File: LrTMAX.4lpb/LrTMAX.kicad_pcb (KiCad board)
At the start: 4 copper layers, 100 x 100 mm, 124 parts, among them J1 USB_B_Micro, J2 SM06B-SRSS-TB, Q1 2N7002, SW1 Tact_SW_8mm, SW10 EC11_SMD, SW11 EC11_SMD, SW12 EC11_SMD, SW13 EC11_SMD, SW14 EC11_SMD, SW15 EC11_SMD, SW16 EC11_SMD, SW17 EC11_SMD, SW2 Tact_SW_8mm, SW3 Tact_SW_8mm, SW4 Tact_SW_8mm, SW5 Tact_SW_8mm, SW6 Tact_SW_8mm, SW7 Tact_SW_8mm, SW8 Tact_SW_8mm, U1 STM32F072C8Tx, U3 SSD1306_OLED_0.91, U4 SPX3819M5-L3-3TR

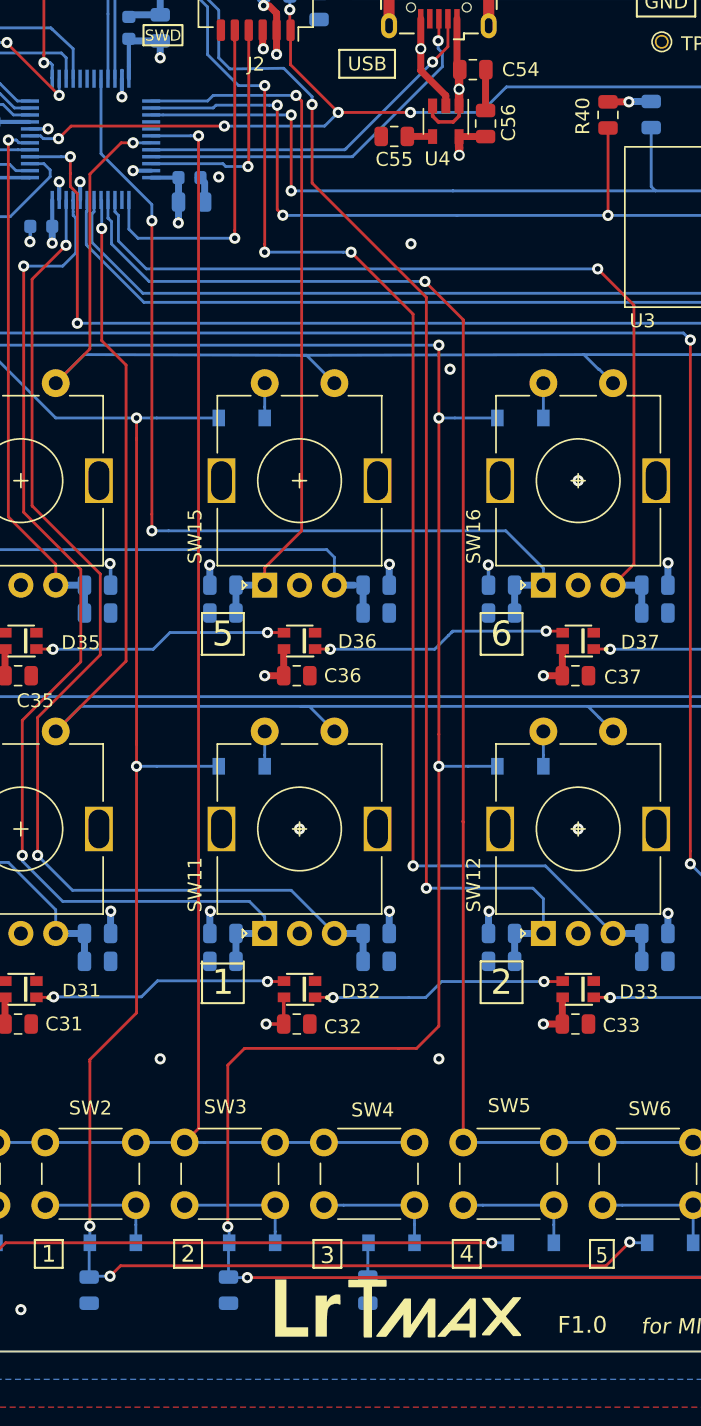
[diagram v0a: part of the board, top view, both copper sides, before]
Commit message: 0.46-4
Fix EXTI routine for ENC3.
(and first modify for F1.2 board)
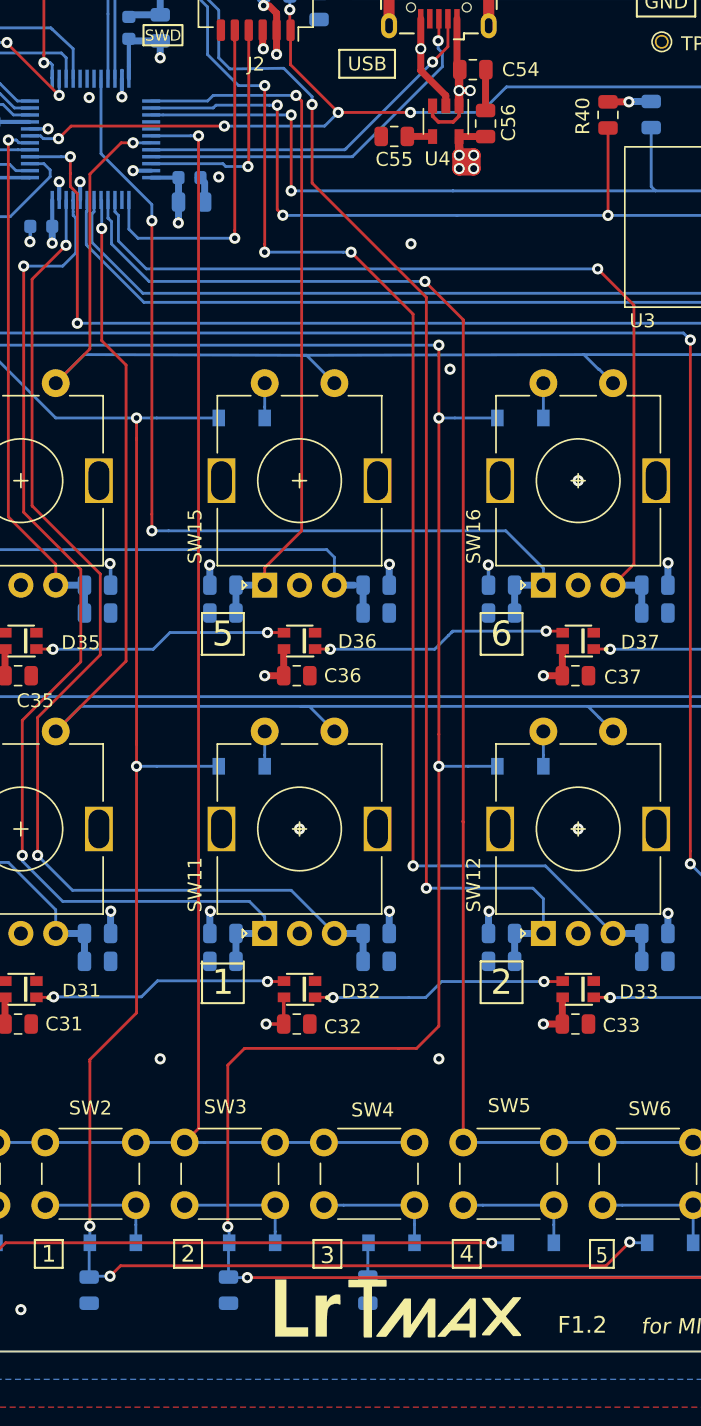
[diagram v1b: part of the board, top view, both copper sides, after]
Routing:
- net +3V3: track 70.1 -> 74.1 mm, vias 27 -> 30
- net /VBUS: track 41.4 -> 42.2 mm, vias 10 -> 11
- net GND: vias 45 -> 46
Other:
- board text added: "F1.2"
- board text removed: "F1.0"
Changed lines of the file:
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@@
     (thickness 1.6)
     (drawings 120)
-    (tracks 992)
+    (tracks 1002)
     (zones 0)
     (modules 124)
@@
     )
   )
-  (gr_text F1.0 (at 160.3 198.1) (layer F.SilkS)
+  (gr_text F1.2 (at 160.3 198.1) (layer F.SilkS)
     (effects (font (size 1.2 1.2) (thickness 0.22)))
   )
@@
   (via (at 134.2 115.7) (size 0.8) (drill 0.4) (layers F.Cu B.Cu) (net 3))
   (via (at 150.8 129.5) (size 0.8) (drill 0.4) (layers F.Cu B.Cu) (net 3))
+  (via (at 124.9 110) (size 0.8) (drill 0.4) (layers F.Cu B.Cu) (net 3))
   (segment (start 178.25 190.914213) (end 178.25 192.2) (width 0.2032) (layer B.Cu) (net 4))
   (segment (start 178.25 189.5) (end 178.25 190.914213) (width 0.2032) (layer B.Cu) (net 4))
@@
   (segment (start 137.5 132.1968) (end 137.5 130.5) (width 0.2032) (layer B.Cu) (net 8))
   (segment (start 137.5 133) (end 137.5 132.1968) (width 0.2032) (layer B.Cu) (net 8))
+  (via (at 152.5 114.141) (size 0.8) (drill 0.5) (layers F.Cu B.Cu) (net 9))
+  (via (at 151.459 115.1) (size 0.8) (drill 0.5) (layers F.Cu B.Cu) (net 9))
+  (via (at 152.5 115.1) (size 0.8) (drill 0.5) (layers F.Cu B.Cu) (net 9))
   (via (at 118.1 113) (size 0.8) (drill 0.4) (layers F.Cu B.Cu) (net 9))
   (via (at 122.25 120.45) (size 0.8) (drill 0.4) (layers F.Cu B.Cu) (net 9))
@@
   (segment (start 173.5625 145) (end 173.5625 143.5625) (width 0.5) (layer B.Cu) (net 9))
   (segment (start 173.5625 143.5625) (end 173.55 143.55) (width 0.254) (layer B.Cu) (net 9))
+  (segment (start 151.459 114.141) (end 151.459 115.1) (width 1) (layer F.Cu) (net 9))
+  (segment (start 151.459 114.141) (end 152.5 114.141) (width 1) (layer F.Cu) (net 9))
+  (segment (start 152.5 114.141) (end 152.5 115.1) (width 1) (layer F.Cu) (net 9))
+  (segment (start 152.5 115.1) (end 151.459 115.1) (width 1) (layer F.Cu) (net 9))
   (segment (start 134.9 192.25) (end 134.95 192.2) (width 0.2032) (layer B.Cu) (net 10))
   (segment (start 134.9 194.6625) (end 134.9 192.25) (width 0.2032) (layer B.Cu) (net 10))
@@
   (segment (start 151.3 104.35) (end 151.3 107.7995) (width 0.5) (layer F.Cu) (net 17) (status 30))
   (segment (start 151.3 107.7995) (end 151.5 108) (width 0.2032) (layer F.Cu) (net 17) (status 30))
-  (via (at 151.45 109.4) (size 0.8) (drill 0.5) (layers F.Cu B.Cu) (net 17))
+  (via (at 151.45 109.5) (size 0.8) (drill 0.5) (layers F.Cu B.Cu) (net 17))
   (segment (start 151.45 110.6) (end 151.45 109.4) (width 0.6) (layer F.Cu) (net 17) (status 10))
   (segment (start 151.45 108.0505) (end 151.5005 108) (width 0.2032) (layer F.Cu) (net 17) (status 30))
@@
   (via (at 117.6 176.5) (size 0.8) (drill 0.4) (layers F.Cu B.Cu) (net 17))
   (segment (start 118.8625 176.5) (end 117.6 176.5) (width 0.5) (layer F.Cu) (net 17))
+  (via (at 152.25 109.5) (size 0.8) (drill 0.5) (layers F.Cu B.Cu) (net 17))
+  (segment (start 151.45 109.5) (end 152.25 109.5) (width 0.5) (layer F.Cu) (net 17))
   (segment (start 149.55 107.45) (end 150.65 106.35) (width 0.2032) (layer F.Cu) (net 18))
   (segment (start 150.65 106.35) (end 150.65 104.35) (width 0.2032) (layer F.Cu) (net 18) (status 20))
@@
   )
   (zone (net 0) (net_name "") (layer F.Cu) (hatch edge 0.508)
-    (connect_pads (clearance 0.3))
-    (min_thickness 0.254)
-    (keepout (tracks allowed) (vias allowed) (copperpour not_allowed))
-    (fill (arc_segments 32) (thermal_gap 0.508) (thermal_bridge_width 0.508))
-    (polygon
-      (pts
-        (xy 150.7 108.2) (xy 150.4 108.2125) (xy 150.1 108.225) (xy 149.5 108.25) (xy 149.5 105.55)
-        (xy 150.7 105.55)
-      )
-    )
-  )
-  (zone (net 0) (net_name "") (layer F.Cu) (hatch edge 0.508)
     (connect_pads (clearance 0.254))
     (min_thickness 0.254)
@@
       )
     )
+  )
+  (zone (net 0) (net_name "") (layer F.Cu) (hatch edge 0.508)
+    (connect_pads (clearance 0.3))
+    (min_thickness 0.254)
+    (keepout (tracks allowed) (vias allowed) (copperpour not_allowed))
+    (fill (arc_segments 32) (thermal_gap 0.508) (thermal_bridge_width 0.508))
+    (polygon
+      (pts
+        (xy 150.7 108.2) (xy 149.4 108.25) (xy 149.4 105.55) (xy 150.7 105.55)
+      )
+    )

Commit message: 0.46-6
LrTMAX.4lpb modify.
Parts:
- moved C50 6.55 mm to (192.5, 120.1)
- moved C49 5.26 mm to (185.2, 121.4)
- moved U3 4.83 mm to (165.0, 109.0)
- moved R42 1.42 mm to (176.6, 120.9)
- moved C47 1.25 mm to (178.4, 119.0)
- moved C45 1.17 mm to (133.3, 115.8)
- moved C46 1.17 mm to (133.4, 117.5)
- moved R44 1.14 mm to (179.3, 121.8)
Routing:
- net GND: track 69.8 -> 80.6 mm, vias 46 -> 65
- net /NRST: track 94.8 -> 91.5 mm
- net +3V3: track 74.1 -> 77.4 mm
- net Net-(C47-Pad2): track 11.5 -> 14.5 mm
- net Net-(R45-Pad1): track 12.6 -> 14.8 mm
- net Net-(C49-Pad2): track 5.96 -> 4.04 mm
- net Net-(C50-Pad2): track 6.47 -> 4.55 mm
- net Net-(C50-Pad1): track 8.89 -> 6.99 mm
- net /SDA: track 68.3 -> 70.1 mm
- net /SCL: track 71.5 -> 73.0 mm
- net Net-(C51-Pad2): track 10.5 -> 11.8 mm
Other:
- outline, holes or cut-outs redrawn

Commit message: 0.46-6
Board F1.2 order.
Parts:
- moved TP1 76.0 mm to (104.0, 150.0)
- moved C50 1.27 mm to (192.5, 121.4)
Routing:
- net /M3: track 203.0 -> 197.1 mm
- net Net-(C50-Pad2): track 4.55 -> 5.82 mm
- net Net-(C50-Pad1): track 6.99 -> 8.26 mm
- net /L3: track 89.2 -> 89.8 mm
- net GND: vias 65 -> 74
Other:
- board text added: "INNER1 LAYER - POWER"
- board text added: "INNER2 LAYER - GND"
- board text added: "PARTS LAYER"
- board text added: "PARTS RESIST"
- board text added: "PARTS SILK"
- board text added: "SOLDER LAYER"
- board text added: "SOLDER RESIST"
- board text added: "SOLDER SILK"

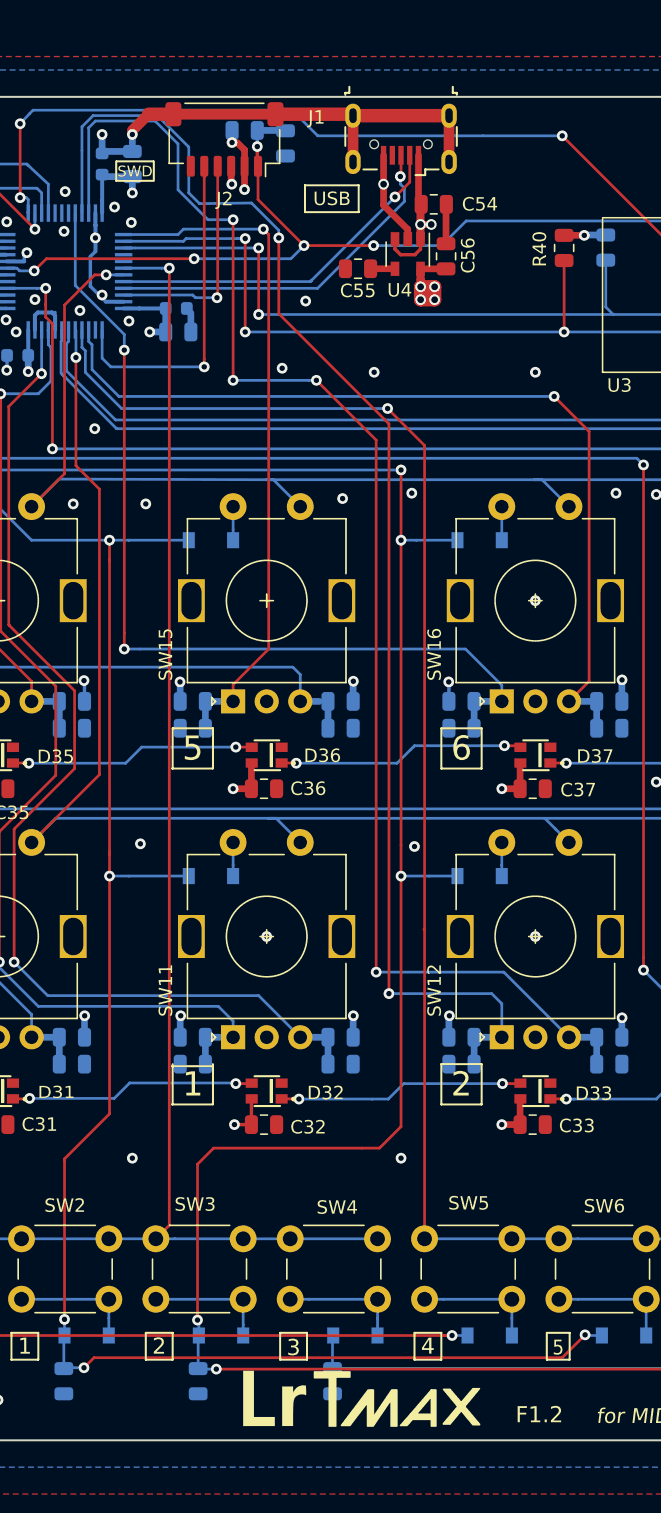
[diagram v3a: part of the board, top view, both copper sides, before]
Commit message: 0.49c
USB conn. changed to typeC
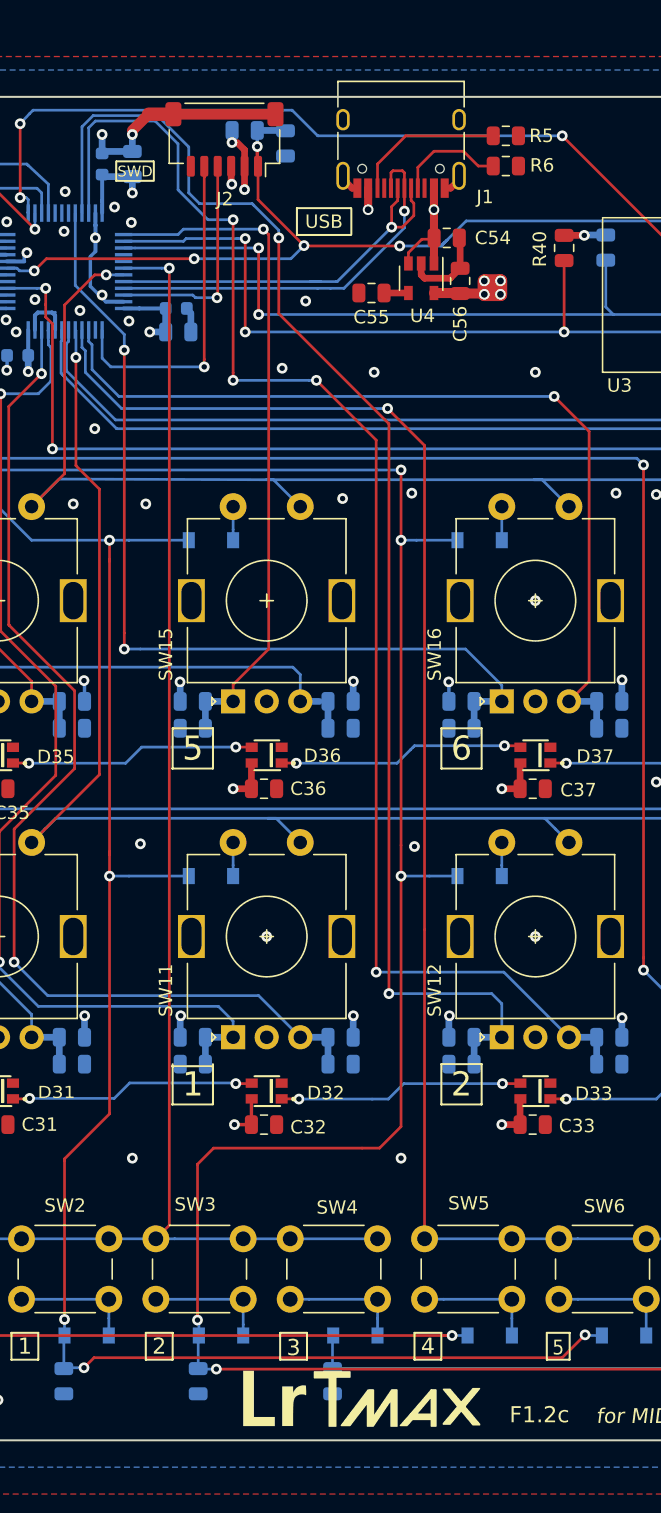
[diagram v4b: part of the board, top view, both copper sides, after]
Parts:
- added R5: 5.1K, Resistor_SMD:R_0805_2012Metric, F.Cu at (157.8, 102.9)
- added R6: 5.1K, Resistor_SMD:R_0805_2012Metric, F.Cu at (157.8, 105.2)
- J1: value USB_B_Micro -> USB_C_Receptacle_USB2.0; footprint LrE-6:USB_Micro-B_MCUBF-09_1 -> Connector_USB:USB_C_Receptacle_HRO_TYPE-C-31-M-12
- R46: value 10K -> 1.2K
- moved C54 2.68 mm to (153.4, 110.5)
- moved C56 2.11 mm to (154.4, 113.7)
- moved C55 2.07 mm to (147.8, 114.6)
- moved U4 2.06 mm to (151.5, 113.5)
- moved J1 0.25 mm to (150.0, 102.8)
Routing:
- net GND: track 80.6 -> 60.5 mm, vias 74 -> 73
- net Net-(J1-PadB5): track 0.00 -> 11.3 mm
- net Net-(J1-PadA5): track 0.00 -> 8.11 mm
- net +3V3: track 77.4 -> 81.8 mm
- net /USB_DM: track 26.5 -> 29.5 mm
- net /USB_DP: track 26.9 -> 28.9 mm
- net /VBUS: track 42.2 -> 40.5 mm
- net /NRST: track 91.5 -> 92.4 mm
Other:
- board text added: "F1.2c"
- board text removed: "F1.2"

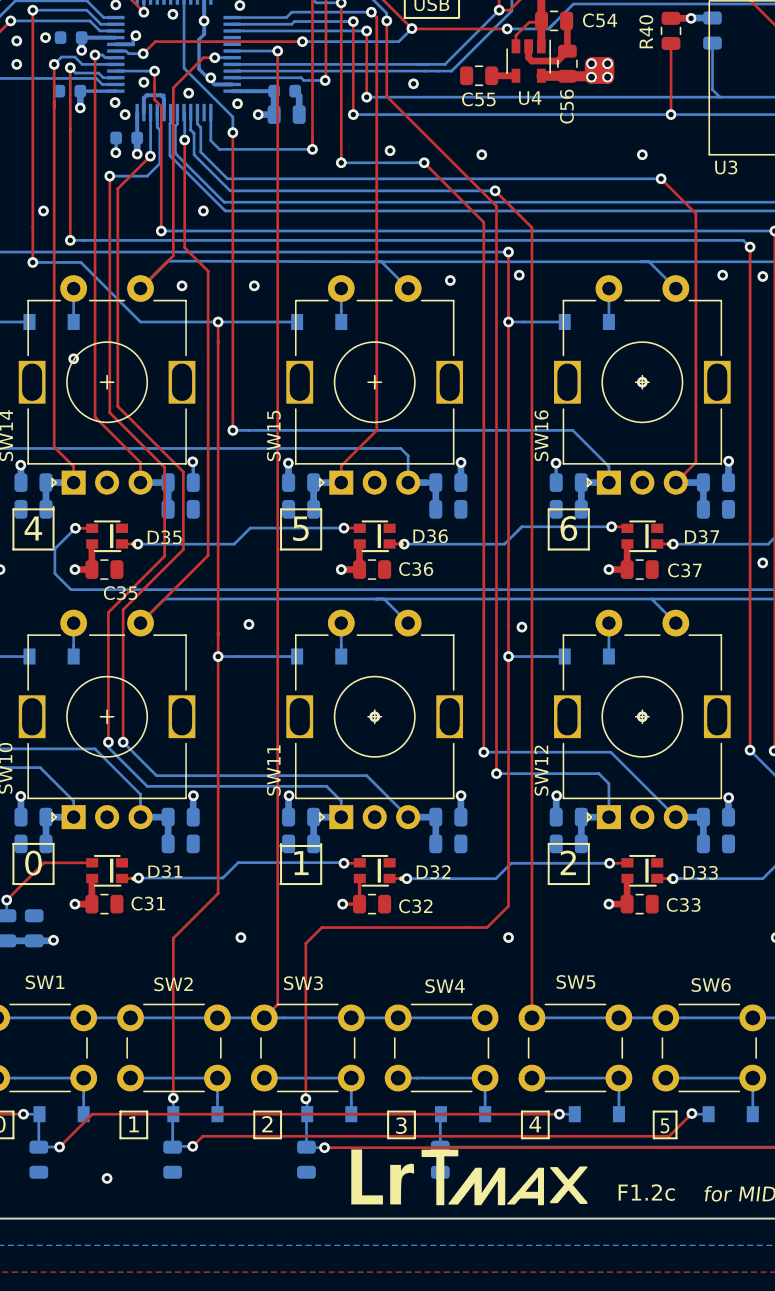
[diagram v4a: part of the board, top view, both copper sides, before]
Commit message: 0.62-00.12cc
Modify "BOOT0" connection on PCB as "1.2cc"
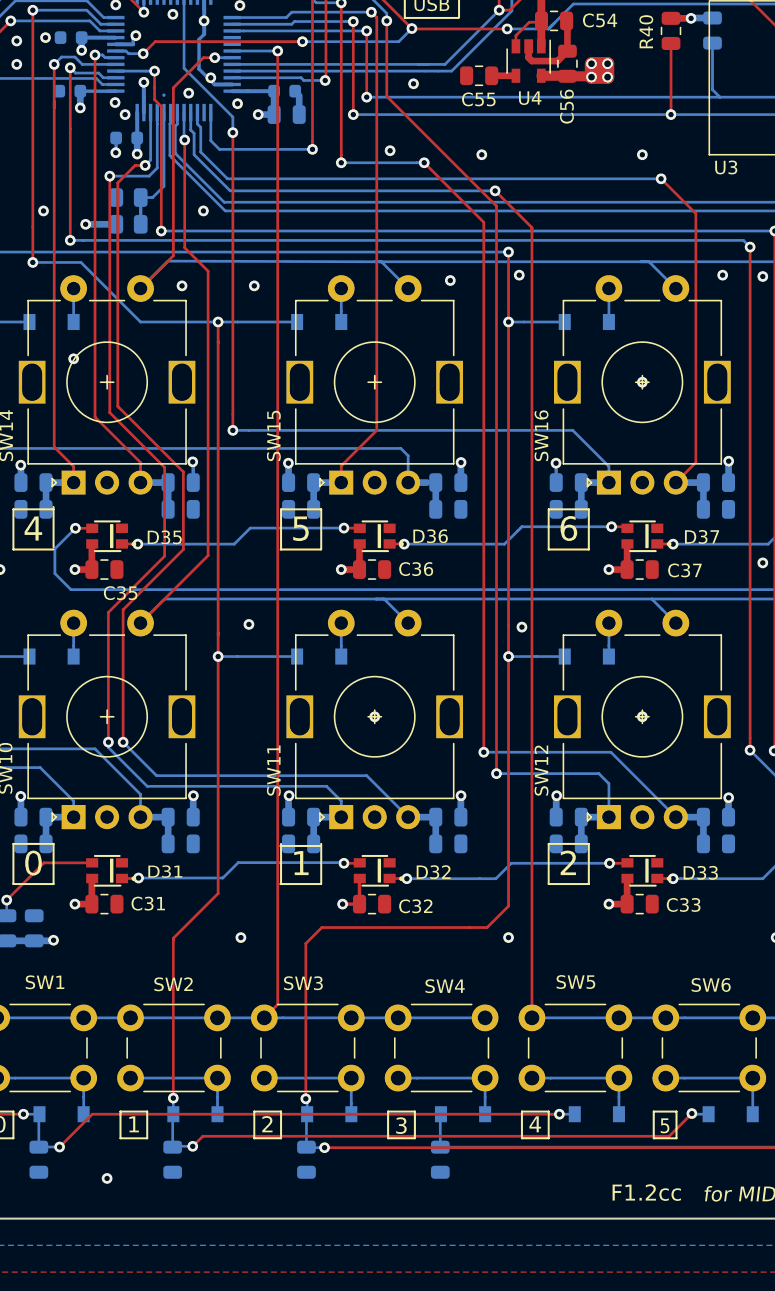
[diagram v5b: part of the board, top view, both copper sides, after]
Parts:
- removed G***: LOGO, LrE-6:Raffles_Inc
- removed REF**: LrTMAX-LOGO, LrE-6:LrTMAX-LOGO
- added R7: 10K, Resistor_SMD:R_0805_2012Metric, B.Cu at (121.6, 125.7)
- added R8: 0, Resistor_SMD:R_0805_2012Metric, B.Cu at (121.6, 123.7)
- C30, C43, C44, C45: value 0.1u -> 100n
- C40, C41, C55: value 10n -> 100n
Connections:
- U1 pad 44: GND -> Net-(R7-Pad2)
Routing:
- net Net-(R7-Pad2): track 0.00 -> 9.59 mm
- net +3V3: track 81.8 -> 84.0 mm, vias 30 -> 31
- net GND: track 60.5 -> 58.9 mm
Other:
- board text added: "F1.2cc"
- board text removed: "F1.2c"
